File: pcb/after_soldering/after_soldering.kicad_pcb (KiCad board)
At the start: 2 copper layers, 181 x 52.4 mm, 39 parts, among them SW11 SW_Push, SW12 SW_Push, SW13 SW_Push, SW17 SW_Push, SW18 SW_Push, SW19 SW_Push, SW3 SW_Push, SW4 SW_Push, SW5 SW_Push, SW7 SW_Push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

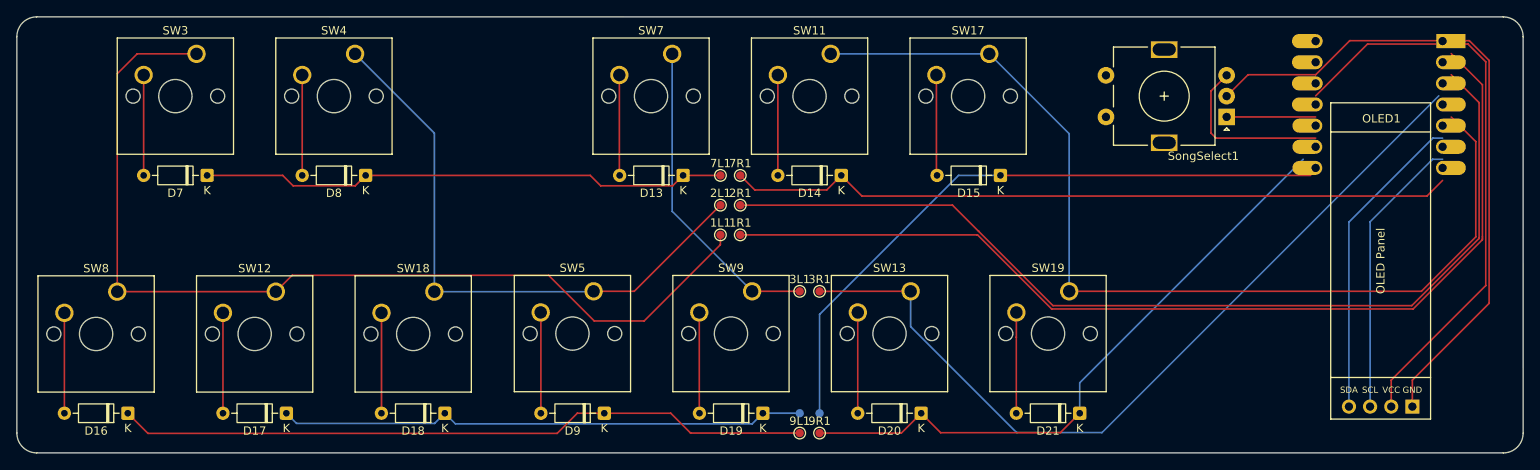
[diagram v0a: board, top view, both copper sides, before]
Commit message: flipping diodes and stuff
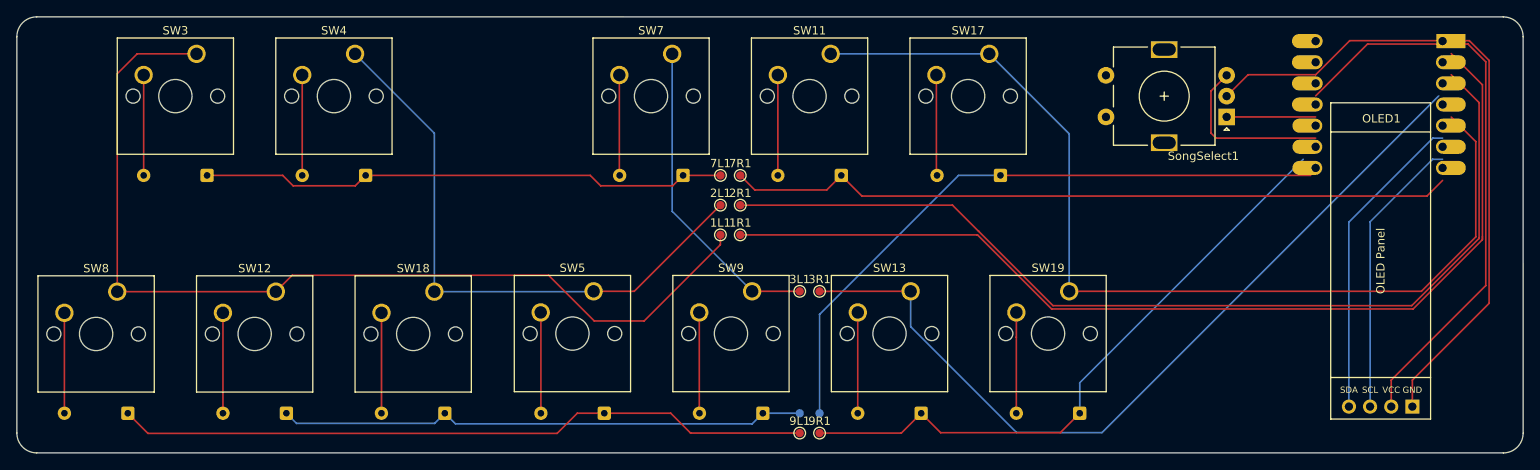
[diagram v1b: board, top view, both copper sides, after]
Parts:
- D13, D14, D15, D16, D17, D18, D19, D20, D21, D7, D8, D9: moved to B.Cu
